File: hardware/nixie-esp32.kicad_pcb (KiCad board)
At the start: 2 copper layers, 62.5 x 47 mm, 56 parts, among them IC1 MCP1661T-E_OT, IC2 CD4504BM, J1 USB4216-03-A_REVA, SW1 RESET, SW2 BOOT, U1 AP7361C-33E-13, U2 ESP32-S3-WROOM-1, U3 SN74AHCT1G125DBVR, U4 HV5622PG

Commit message: Nate's bad attempt at routing traces
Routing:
- net +170V: track 0.00 -> 63.3 mm, vias 0 -> 6
- net +5V: track 0.00 -> 36.2 mm
- net Net-(J1-VBUS_A): track 0.00 -> 21.8 mm
- net /Nixies/HvDriver/Nixie3/K3: track 0.00 -> 18.9 mm
- net /Nixies/HvDriver/Nixie3/K2: track 0.00 -> 15.9 mm
- net /Nixies/HvDriver/Nixie3/K1: track 0.00 -> 15.6 mm
- net /Nixies/HvDriver/Nixie1/ANODE: track 0.00 -> 10.1 mm, vias 0 -> 1
- net Net-(D5-A): track 0.00 -> 9.72 mm
- net /Nixies/HvDriver/Nixie3/ANODE: track 0.00 -> 8.06 mm, vias 0 -> 1
- net /USB_D+: track 0.00 -> 6.61 mm, vias 0 -> 1
- net +12V: track 0.00 -> 4.87 mm
- net Net-(IC1-VFB): track 0.00 -> 4.68 mm
- added copper zone on B.Cu, net GND
- added copper zone on F.Cu, net GND

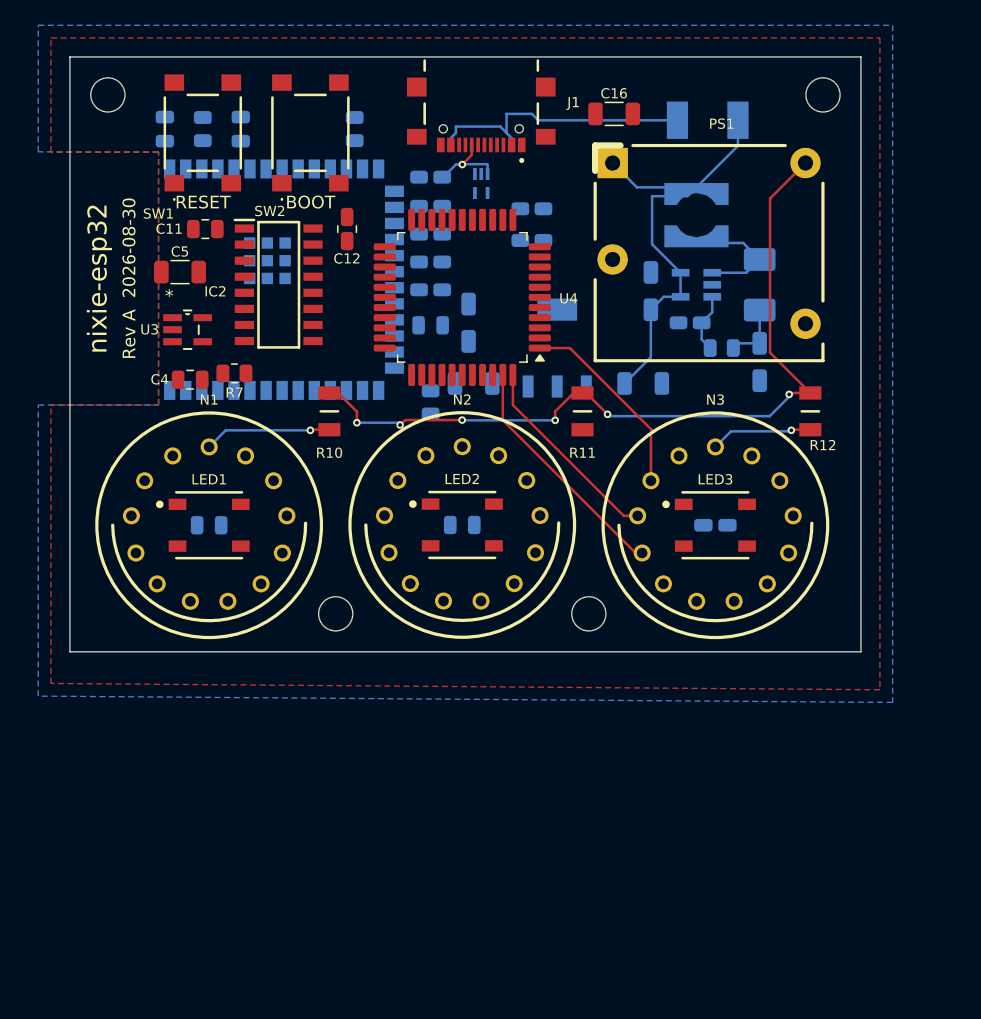
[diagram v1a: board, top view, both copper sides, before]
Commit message: Route all nixie cathodes and anodes
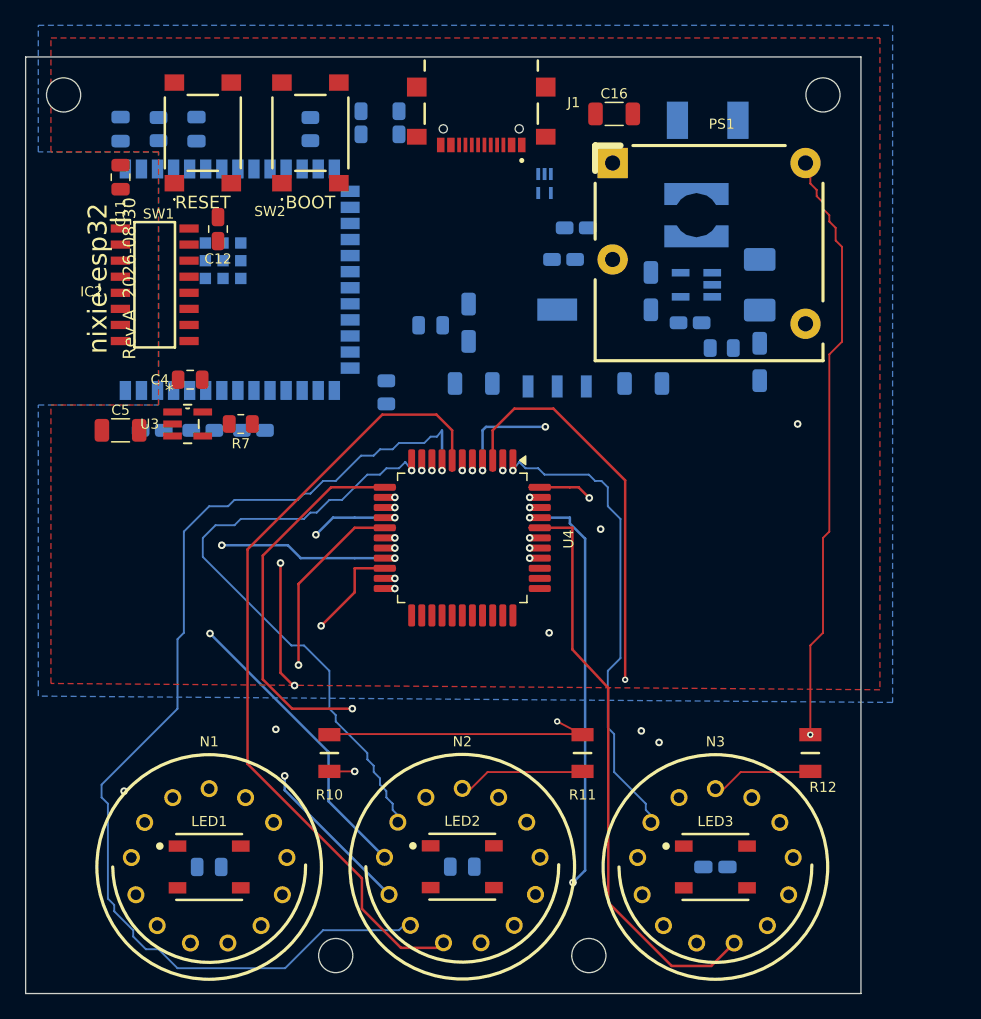
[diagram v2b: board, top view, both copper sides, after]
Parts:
- moved LED2 27.0 mm to (151.5, 140.5)
- moved N2 27.0 mm to (151.5, 140.5)
- moved C6 27.0 mm to (131.5, 140.5)
- moved C8 27.0 mm to (171.5, 140.5)
- moved H3 27.0 mm to (141.5, 147.5)
- moved H4 27.0 mm to (161.5, 147.5)
- moved LED1 27.0 mm to (131.5, 140.5)
- moved LED3 27.0 mm to (171.5, 140.5)
- moved N1 27.0 mm to (131.5, 140.5)
- moved N3 27.0 mm to (171.5, 140.5)
- moved R10 27.0 mm to (141.0, 131.5)
- moved R11 27.0 mm to (161.0, 131.5)
- moved R12 27.0 mm to (179.0, 131.5)
- moved C7 27.0 mm to (151.5, 140.5)
- moved R15 26.9 mm to (127.0, 106.0)
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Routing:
- net /Nixies/HvDriver/Nixie2/K6: track 0.00 -> 98.8 mm, vias 0 -> 1
- net /Nixies/HvDriver/Nixie2/K4: track 0.00 -> 87.8 mm, vias 0 -> 1
- net /Nixies/HvDriver/Nixie2/K5: track 0.00 -> 65.1 mm
- net /Nixies/HvDriver/Nixie2/K7: track 0.00 -> 61.9 mm, vias 0 -> 2
- net /Nixies/HvDriver/Nixie3/K0: track 0.00 -> 59.7 mm, vias 0 -> 2
- net /Nixies/HvDriver/Nixie3/K9: track 0.00 -> 53.0 mm, vias 0 -> 1
- net /Nixies/HvDriver/Nixie2/K8: track 0.00 -> 52.7 mm, vias 0 -> 3
- net /Nixies/HvDriver/Nixie2/K3: track 0.00 -> 52.7 mm, vias 0 -> 2
- net /Nixies/HvDriver/Nixie2/K2: track 0.00 -> 51.9 mm, vias 0 -> 2
- net /Nixies/HvDriver/Nixie1/K5: track 0.00 -> 51.8 mm, vias 0 -> 1
- net /Nixies/HvDriver/Nixie2/K0: track 0.00 -> 50.1 mm, vias 0 -> 1
- net /Nixies/HvDriver/Nixie2/K9: track 0.00 -> 50.1 mm, vias 0 -> 1
- net /Nixies/HvDriver/Nixie1/K4: track 0.00 -> 50.0 mm, vias 0 -> 1
- net /Nixies/HvDriver/Nixie2/K1: track 0.00 -> 49.6 mm, vias 0 -> 1
- net /Nixies/HvDriver/Nixie3/K6: track 0.00 -> 47.7 mm
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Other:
- board size 62.5 x 47 mm -> 66 x 74 mm
- copper layers 2 -> 6

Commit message: WIP SN74141 redesign
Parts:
- removed C10, C14, C9: 10µF, Capacitor_SMD:C_1206_3216Metric
- removed D5: SS14-HF, Diode_SMD:D_SMA
- removed IC1: MCP1661T-E_OT, nixie-esp32:SOT95P270X145-5N
- removed IC2: CD4504BM, nixie-esp32:SOIC127P600X175-16N
- removed L1: 4.7µH, nixie-esp32:MSS5131
- removed R8: 1.05M, Resistor_SMD:R_0805_2012Metric
- removed R9: 120k, Resistor_SMD:R_0805_2012Metric
- added U5: SN74141N, Package_DIP:DIP-16_W7.62mm, F.Cu at (142.6, 114.5)
- added U6: SN74141N, Package_DIP:DIP-16_W7.62mm, F.Cu at (163.6, 114.5)
- C11, C12: moved to B.Cu
- U4: value HV5622PG -> SN74141N; footprint Package_QFP:PQFP-44_10x10mm_P0.8mm -> Package_DIP:DIP-16_W7.62mm
- moved C12 33.9 mm to (152.8, 117.0), turned to 180 degrees
- moved C11 31.8 mm to (131.8, 117.0), turned to 180 degrees
- moved C13 31.4 mm to (173.8, 117.0), turned to 180 degrees
- moved U4 29.9 mm to (121.6, 114.5), turned to 90 degrees
- moved R15 26.9 mm to (149.0, 90.5)
- moved R16 22.4 mm to (149.0, 92.7)
- moved R13 17.9 mm to (149.0, 94.9)
- moved C6 13.5 mm to (130.5, 127.0)
- moved C8 13.5 mm to (172.5, 127.0)
- moved LED1 13.5 mm to (130.5, 127.0)
- moved LED3 13.5 mm to (172.5, 127.0)
- moved N1 13.5 mm to (130.5, 127.0)
- moved N3 13.5 mm to (172.5, 127.0)
- moved H3 13.5 mm to (141.0, 134.0)
- moved H4 13.5 mm to (162.0, 134.0)
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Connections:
- C12 pad 1: +12V -> +5V
- C13 pad 1: GND -> +5V
- C13 pad 2: +12V -> GND
- N1 pad 0: /Nixies/HvDriver/Nixie1/K0 -> /Nixies/HvDriver/N1_K0
- N1 pad 1: /Nixies/HvDriver/Nixie1/K1 -> /Nixies/HvDriver/N1_K1
- N1 pad 2: /Nixies/HvDriver/Nixie1/K2 -> /Nixies/HvDriver/N1_K2
- N1 pad 3: /Nixies/HvDriver/Nixie1/K3 -> /Nixies/HvDriver/N1_K3
- N1 pad 4: /Nixies/HvDriver/Nixie1/K4 -> /Nixies/HvDriver/N1_K4
- N1 pad 5: /Nixies/HvDriver/Nixie1/K5 -> /Nixies/HvDriver/N1_K5
- N1 pad 6: /Nixies/HvDriver/Nixie1/K6 -> /Nixies/HvDriver/N1_K6
- N1 pad 7: /Nixies/HvDriver/Nixie1/K7 -> /Nixies/HvDriver/N1_K7
- N1 pad 8: /Nixies/HvDriver/Nixie1/K8 -> /Nixies/HvDriver/N1_K8
- N1 pad 9: /Nixies/HvDriver/Nixie1/K9 -> /Nixies/HvDriver/N1_K9
- N2 pad 0: /Nixies/HvDriver/Nixie2/K0 -> /Nixies/HvDriver/N2_K0
- N2 pad 1: /Nixies/HvDriver/Nixie2/K1 -> /Nixies/HvDriver/N2_K1
- N2 pad 2: /Nixies/HvDriver/Nixie2/K2 -> /Nixies/HvDriver/N2_K2
- N2 pad 3: /Nixies/HvDriver/Nixie2/K3 -> /Nixies/HvDriver/N2_K3
- N2 pad 4: /Nixies/HvDriver/Nixie2/K4 -> /Nixies/HvDriver/N2_K4
- N2 pad 5: /Nixies/HvDriver/Nixie2/K5 -> /Nixies/HvDriver/N2_K5
- N2 pad 6: /Nixies/HvDriver/Nixie2/K6 -> /Nixies/HvDriver/N2_K6
- N2 pad 7: /Nixies/HvDriver/Nixie2/K7 -> /Nixies/HvDriver/N2_K7
- N2 pad 8: /Nixies/HvDriver/Nixie2/K8 -> /Nixies/HvDriver/N2_K8
- N2 pad 9: /Nixies/HvDriver/Nixie2/K9 -> /Nixies/HvDriver/N2_K9
- N3 pad 0: /Nixies/HvDriver/Nixie3/K0 -> /Nixies/HvDriver/N3_K0
- N3 pad 1: /Nixies/HvDriver/Nixie3/K1 -> /Nixies/HvDriver/N3_K1
- N3 pad 2: /Nixies/HvDriver/Nixie3/K2 -> /Nixies/HvDriver/N3_K2
- N3 pad 3: /Nixies/HvDriver/Nixie3/K3 -> /Nixies/HvDriver/N3_K3
- N3 pad 4: /Nixies/HvDriver/Nixie3/K4 -> /Nixies/HvDriver/N3_K4
- N3 pad 5: /Nixies/HvDriver/Nixie3/K5 -> /Nixies/HvDriver/N3_K5
- N3 pad 6: /Nixies/HvDriver/Nixie3/K6 -> /Nixies/HvDriver/N3_K6
- N3 pad 7: /Nixies/HvDriver/Nixie3/K7 -> /Nixies/HvDriver/N3_K7
- N3 pad 8: /Nixies/HvDriver/Nixie3/K8 -> /Nixies/HvDriver/N3_K8
- N3 pad 9: /Nixies/HvDriver/Nixie3/K9 -> /Nixies/HvDriver/N3_K9
- U2 pad 10: unconnected-(U2-GPIO17/U1TXD/ADC2_CH6-Pad10) -> ESP32_GPIO17
- U2 pad 11: unconnected-(U2-GPIO18/U1RXD/ADC2_CH7/CLK_OUT3-Pad11) -> ESP32_GPIO18
- U2 pad 20: unconnected-(U2-GPIO12/TOUCH12/ADC2_CH1/FSPICLK/FSPIIO6/SUBSPICLK-Pad20) -> ESP32_GPIO12
- U2 pad 21: unconnected-(U2-GPIO13/TOUCH13/ADC2_CH2/FSPIQ/FSPIIO7/SUBSPIQ-Pad21) -> ESP32_GPIO13
- U2 pad 22: unconnected-(U2-GPIO14/TOUCH14/ADC2_CH3/FSPIWP/FSPIDQS/SUBSPIWP-Pad22) -> ESP32_GPIO14
- U2 pad 23: unconnected-(U2-GPIO21-Pad23) -> ESP32_GPIO21
- U2 pad 31: unconnected-(U2-GPIO38/FSPIWP/SUBSPIWP-Pad31) -> ESP32_GPIO38
- U2 pad 38: unconnected-(U2-GPIO2/TOUCH2/ADC1_CH1-Pad38) -> ESP32_GPIO2
- U2 pad 39: unconnected-(U2-GPIO1/TOUCH1/ADC1_CH0-Pad39) -> ESP32_GPIO1
- U2 pad 5: unconnected-(U2-GPIO5/TOUCH5/ADC1_CH4-Pad5) -> ESP32_GPIO5
- U2 pad 6: unconnected-(U2-GPIO6/TOUCH6/ADC1_CH5-Pad6) -> ESP32_GPIO6
- U2 pad 7: unconnected-(U2-GPIO7/TOUCH7/ADC1_CH6-Pad7) -> ESP32_GPIO7
- U4 pad 1: /Nixies/HvDriver/Nixie3/K1 -> /Nixies/HvDriver/N1_K8
- U4 pad 10: /Nixies/HvDriver/Nixie2/K2 -> /Nixies/HvDriver/N1_K7
- U4 pad 11: /Nixies/HvDriver/Nixie2/K1 -> /Nixies/HvDriver/N1_K6
- U4 pad 12: /Nixies/HvDriver/Nixie2/K0 -> GND
- U4 pad 13: /Nixies/HvDriver/Nixie1/K9 -> /Nixies/HvDriver/N1_K4
- U4 pad 14: /Nixies/HvDriver/Nixie1/K8 -> /Nixies/HvDriver/N1_K5
- U4 pad 15: /Nixies/HvDriver/Nixie1/K7 -> /Nixies/HvDriver/N1_K0
- U4 pad 16: /Nixies/HvDriver/Nixie1/K6 -> /Nixies/HvDriver/N1_K2
- U4 pad 2: /Nixies/HvDriver/Nixie3/K0 -> /Nixies/HvDriver/N1_K9
- U4 pad 3: /Nixies/HvDriver/Nixie2/K9 -> ESP32_GPIO1
- U4 pad 4: /Nixies/HvDriver/Nixie2/K8 -> ESP32_GPIO6
- U4 pad 5: /Nixies/HvDriver/Nixie2/K7 -> +5V
- U4 pad 6: /Nixies/HvDriver/Nixie2/K6 -> ESP32_GPIO2
- U4 pad 7: /Nixies/HvDriver/Nixie2/K5 -> ESP32_GPIO5
- U4 pad 8: /Nixies/HvDriver/Nixie2/K4 -> /Nixies/HvDriver/N1_K1
- U4 pad 9: /Nixies/HvDriver/Nixie2/K3 -> /Nixies/HvDriver/N1_K3
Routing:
- net /Nixies/HvDriver/Nixie2/K6: track 98.8 -> 0.00 mm, vias 1 -> 0
- net +170V: track 90.8 -> 0.00 mm, vias 2 -> 0
- net /Nixies/HvDriver/Nixie2/K4: track 87.8 -> 0.00 mm, vias 1 -> 0
- net /Nixies/HvDriver/Nixie2/K5: track 65.1 -> 0.00 mm
- net /Nixies/HvDriver/Nixie2/K7: track 61.9 -> 0.00 mm, vias 2 -> 0
- net /Nixies/HvDriver/Nixie3/K0: track 59.7 -> 0.00 mm, vias 2 -> 0
- net /Nixies/HvDriver/Nixie3/K9: track 53.0 -> 0.00 mm, vias 1 -> 0
- net /Nixies/HvDriver/Nixie2/K8: track 52.7 -> 0.00 mm, vias 3 -> 0
- net /Nixies/HvDriver/Nixie2/K3: track 52.7 -> 0.00 mm, vias 2 -> 0
- net /Nixies/HvDriver/Nixie2/K2: track 51.9 -> 0.00 mm, vias 2 -> 0
- net /Nixies/HvDriver/Nixie1/K5: track 51.8 -> 0.00 mm, vias 1 -> 0
- net /Nixies/HvDriver/Nixie2/K0: track 50.1 -> 0.00 mm, vias 1 -> 0
- net /Nixies/HvDriver/Nixie2/K9: track 50.1 -> 0.00 mm, vias 1 -> 0
- net /Nixies/HvDriver/Nixie1/K4: track 50.0 -> 0.00 mm, vias 1 -> 0
- net /Nixies/HvDriver/Nixie2/K1: track 49.6 -> 0.00 mm, vias 1 -> 0
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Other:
- board size 66 x 74 mm -> 65 x 60.5 mm
- copper layers 6 -> 2

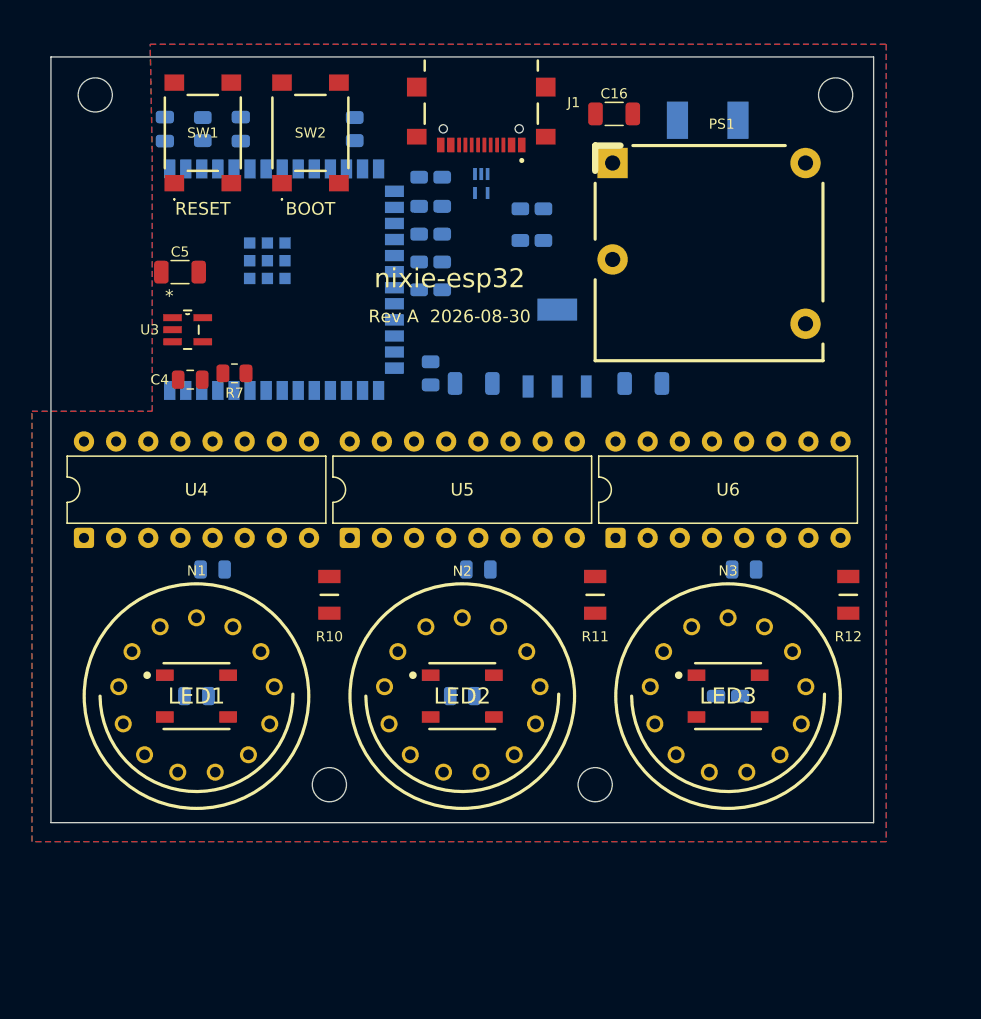
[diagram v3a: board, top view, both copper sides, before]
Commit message: Route display subsystem on six layers
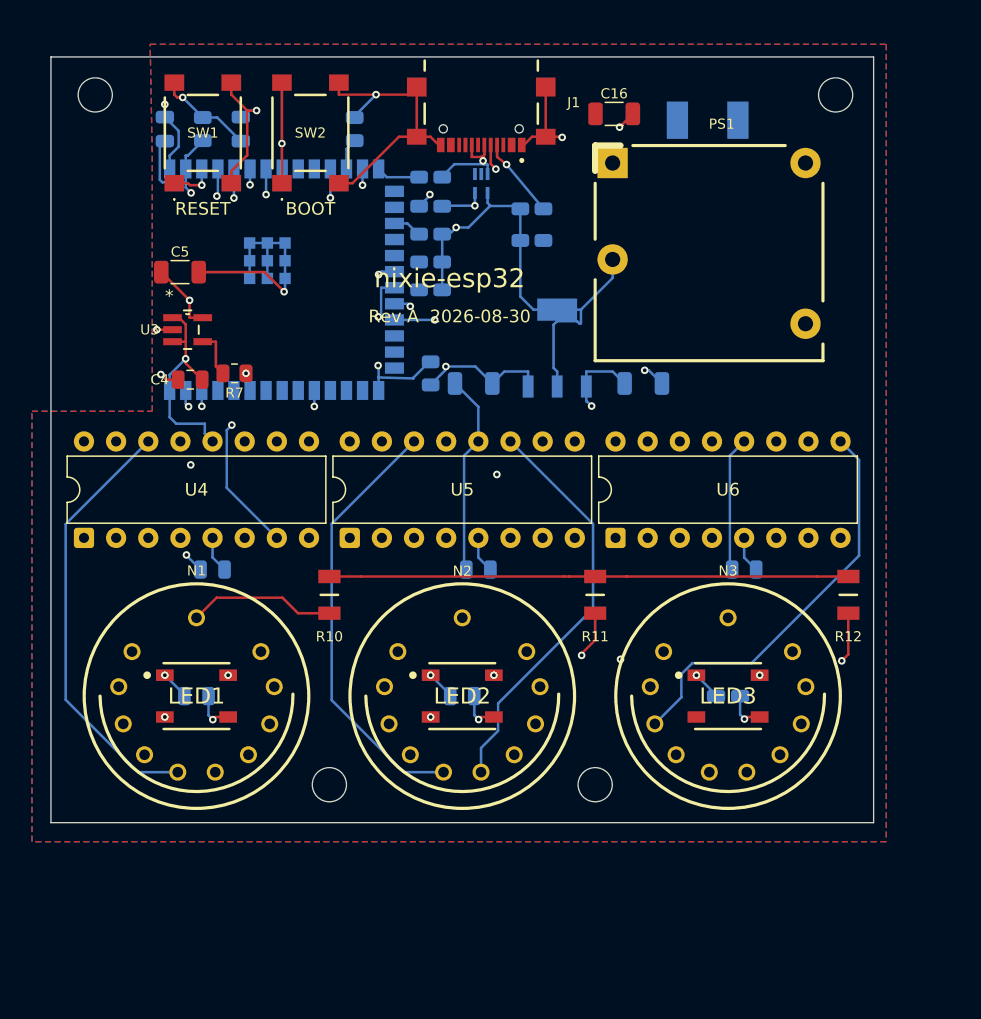
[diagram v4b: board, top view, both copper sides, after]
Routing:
- net GND: track 0.00 -> 353.7 mm, vias 0 -> 13
- net +5V: track 0.00 -> 188.4 mm, vias 0 -> 6
- net ESP32_GPIO18: track 0.00 -> 49.1 mm, vias 0 -> 1
- net /Nixies/HvDriver/N2_K2: track 0.00 -> 47.9 mm
- net /Nixies/HvDriver/N3_K2: track 0.00 -> 47.9 mm
- net +3.3V: track 0.00 -> 46.7 mm, vias 0 -> 2
- net /Nixies/HvDriver/N1_K6: track 0.00 -> 45.4 mm
- net ESP32_GPIO21: track 0.00 -> 41.0 mm, vias 0 -> 1
- net +170V: track 0.00 -> 41.0 mm
- net /Nixies/HvDriver/N1_K8: track 0.00 -> 38.9 mm
- net ESP32_GPIO38: track 0.00 -> 37.6 mm, vias 0 -> 1
- net Net-(SW2-NO_1): track 0.00 -> 35.3 mm, vias 0 -> 2
- net /Nixies/HvDriver/N3_K6: track 0.00 -> 34.8 mm
- net /Nixies/HvDriver/N1_K5: track 0.00 -> 34.3 mm
- net /Nixies/HvDriver/N2_K5: track 0.00 -> 34.3 mm
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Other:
- copper layers 2 -> 6

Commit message: Expand board and remove display jumpers
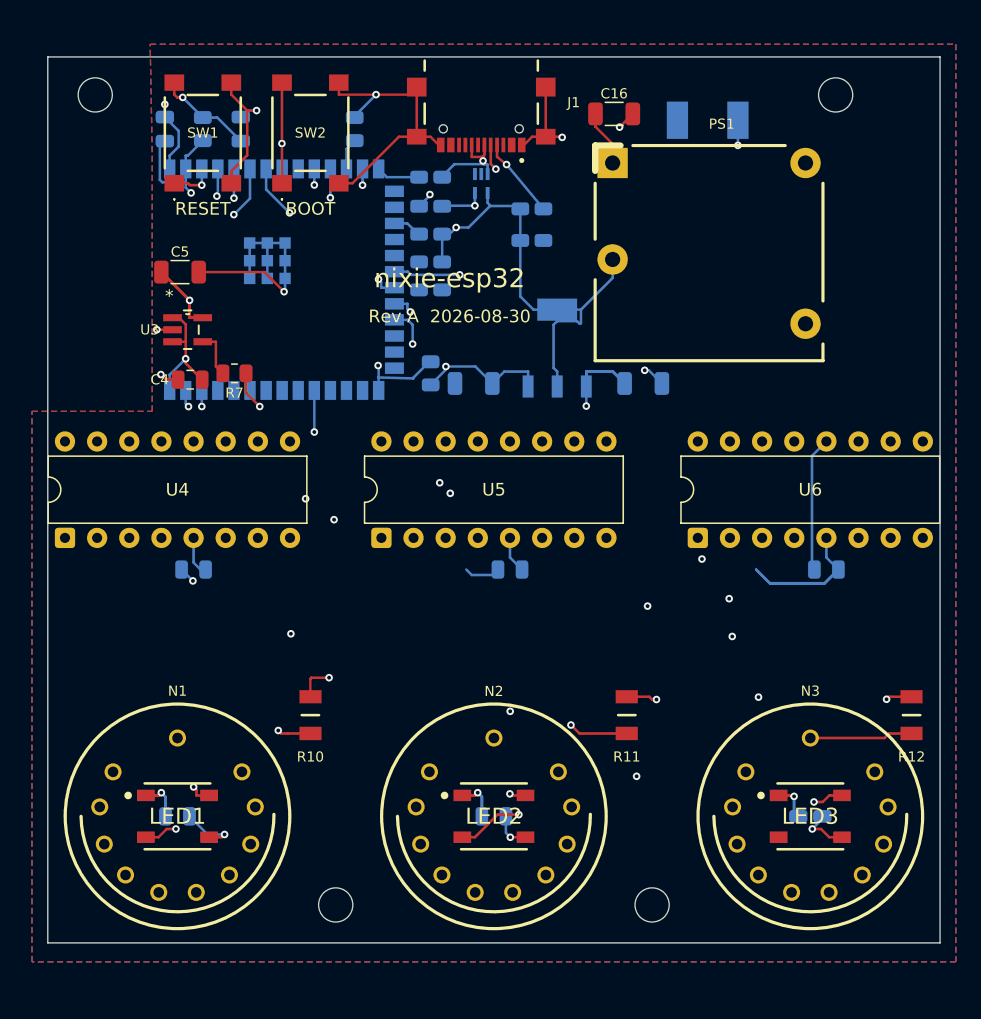
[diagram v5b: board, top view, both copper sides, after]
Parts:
- moved C8 11.5 mm to (179.0, 136.5)
- moved LED3 11.5 mm to (179.0, 136.5)
- moved N3 11.5 mm to (179.0, 136.5)
- moved R12 10.7 mm to (187.0, 128.5)
- moved H4 10.5 mm to (166.5, 143.5)
- moved C7 9.82 mm to (154.0, 136.5)
- moved LED2 9.82 mm to (154.0, 136.5)
- moved N2 9.82 mm to (154.0, 136.5)
- moved R11 9.82 mm to (164.5, 128.5)
- moved C6 9.62 mm to (129.0, 136.5)
- moved LED1 9.62 mm to (129.0, 136.5)
- moved N1 9.62 mm to (129.0, 136.5)
- moved R10 9.62 mm to (139.5, 128.5)
- moved H3 9.51 mm to (141.5, 143.5)
- moved C13 6.50 mm to (180.3, 117.0)
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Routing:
- net +5V: track 188.4 -> 292.0 mm, vias 6 -> 7
- net +170V: track 41.0 -> 101.2 mm, vias 0 -> 4
- net /Nixies/HvDriver/N3_K4: track 0.00 -> 51.6 mm, vias 0 -> 1
- net ESP32_GPIO17: track 0.00 -> 51.5 mm, vias 0 -> 1
- net /Nixies/HvDriver/N2_K3: track 0.00 -> 49.0 mm, vias 0 -> 1
- net /Nixies/HvDriver/N2_K4: track 0.00 -> 43.9 mm, vias 0 -> 1
- net GND: track 353.7 -> 310.3 mm
- net /Nixies/HvDriver/N1_K2: track 21.8 -> 50.8 mm
- net /Nixies/HvDriver/N3_K7: track 29.3 -> 56.0 mm
- net ESP32_GPIO6: track 31.5 -> 56.1 mm, vias 1 -> 2
- net /Nixies/HvDriver/N1_K5: track 34.3 -> 55.1 mm, vias 0 -> 1
- net /LEDs/LED1_DIN: track 32.5 -> 52.1 mm
- net /Nixies/HvDriver/N3_K6: track 34.8 -> 53.9 mm
- net /Nixies/HvDriver/N3_K3: track 32.3 -> 50.0 mm, vias 0 -> 1
- net /Nixies/HvDriver/N2_K2: track 47.9 -> 31.8 mm
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- added copper zone on In1.Cu, net +5V
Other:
- board size 65 x 60.5 mm -> 70.5 x 70 mm

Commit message: Route remaining board connections
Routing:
- net +5V: track 292.0 -> 248.2 mm
- net Net-(J1-VBUS_A): track 0.00 -> 26.5 mm, vias 0 -> 2
- net Net-(J1-CC2): track 0.00 -> 16.5 mm, vias 0 -> 2
- net /ESP32_GPIO11: track 0.00 -> 8.13 mm, vias 0 -> 2
- net /ESP32_GPIO10: track 0.00 -> 3.20 mm
- net /USB_D-: track 9.27 -> 12.0 mm
- net GND: track 310.3 -> 307.8 mm

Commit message: Align board with JLCPCB capabilities
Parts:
- added TP1: GND, , F.Cu at (165.9, 101.3)
- added TP2: +3.3V, , F.Cu at (150.2, 101.0)
- added TP3: +5V, , F.Cu at (161.3, 104.1)
- added TP4: +170V, , F.Cu at (166.1, 119.9)
- renumbered LED1 to D2, LED2 to D3, LED3 to D4
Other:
- board text added: "+170V"
- board text added: "+3V3"
- board text added: "+5V"
- board text added: "GND"
